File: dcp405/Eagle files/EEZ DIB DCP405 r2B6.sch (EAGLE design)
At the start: 316 parts, among them IC1 LTC3864EMSE#PBF, IC10 MC33272ADR2G, IC11 LTC2050HVCS8#PBF, IC12 74AUP1G74DC.125, IC13 MCP23S17-E/SS, IC14 TC77-5.0MCTTR, IC15 REF5025AIDR, IC16 DAC8552IDGKR, IC17 SN74LVC1G3157DCKR, IC18 ADS1120IPWR, IC19 LM339D, IC2 TPS54060DGQ, IC20 MAX9141ESA, IC3 SI8641BB-B-IS1, IC4 SN74LVC1G139DCUR, IC5 MC78L05, IC6 MC79L05, IC7 SI8641BB-B-IS1, IC8 M24C32-WMN6P, IC9 OPA2196ID, J1 4907, J2 FCR7350R, J3 FCR7350B, K1 G6K-2F-5DC, Q1 SUD19P06-60, Q10 BSS205NH6327XTSA1, Q11 PSMN0R9-25YLC, Q12 PSMN0R9-25YLC, Q13 BSS84P, Q14 BTA26-600, Q15 FMMT493TA, Q16 2N7002, Q17 2N7002, Q18 2N7002, Q19 MMBT5551, Q2 MMBT5401, Q20 MMBT5401, Q21 MMBT5551, Q22 MMBT5551, Q23 2N7002, Q3 D45H11, Q4 D45H11, Q5 BC856C, Q6 MMBT5401, Q7 STF10P6F6, Q8 BCP56-16.115, Q9 NZT605, Q9B BDX33C, X1 39-30-1020, X2 77317-104-28LF, X3 1844249, X4 DS1024-2*10R0

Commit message: DCP405 r2B6 (w/o BOM)
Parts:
- removed D20: SK10100D1-DIO, EEZ_Lib1:SCHOTTKY-DUAL_A_L
- removed D21: BAS316, EEZ_Lib1:DIODESOD323R
- removed JP2: JP3-CUT-ROTATED, EEZ_Lib1:JP3-CUT-ROTATED
- removed JP3: JP3-CUT, EEZ_Lib1:JP3-CUT
- removed Q23: 2N7002, EEZ_Lib1:2N7002
- removed Q9B: BDX33C, EEZ_Lib1:BDX33C
- removed R111: 750R, rcl:R-EU_R0805
- removed R112: 47K, rcl:R-EU_R0805
- removed R113: 330R, rcl:R-EU_R0805
- removed R114: 470R, rcl:R-EU_R0805
- removed R115: 100K, rcl:R-EU_R0805
- added C96: 10n, rcl:C-EUC0805
- added ZD3: SLVU2.8-TP, EEZ_Lib1:SLVU2.8
- C29: value 100n -> 10n; device rcl:C-EUC0603 -> rcl:C-EUC0805
- C41: value 47p -> 470p
- C43: value 470p -> 33p
- C44: value 2n2 -> 330p
- C45: value 220p -> 2n2
- C46: value 47p -> 33p
- C47: value 470p -> 10n
- C48, C70, C86: value 10n -> 100n; device rcl:C-EUC0805 -> rcl:C-EUC0603
- C51, C67, C77, C79: value 100n -> 1u; device rcl:C-EUC0603 -> rcl:C-EUC0805
- C52: value 1u -> 10n
- C53: value 10n -> 1n
- C54: value 1n -> 1u
- C55, C76, C78: value 1u -> 100n; device rcl:C-EUC0805 -> rcl:C-EUC0603
- C58: value 100n -> 33p; device rcl:C-EUC0603 -> rcl:C-EUC0805
- C60: value 100n -> 100p; device rcl:C-EUC0603 -> rcl:C-EUC0805
- C62: value 4u7 -> 100n; device rcl:C-EUC1206 -> rcl:C-EUC0603
- C63: value 100n -> 4u7; device rcl:C-EUC0603 -> rcl:C-EUC1206
- C64: value 4u7 tant. -> 100n; device EEZ_Lib1:ECAP1206 -> rcl:C-EUC0603
- C65: value 1u -> 4u7 tant.; device rcl:C-EUC0805 -> EEZ_Lib1:ECAP1206
- C71: value 4n7 -> 10n
- C75: value 100n -> 4n7; device rcl:C-EUC0603 -> rcl:C-EUC0805
- C84: value 100n -> 1n; device rcl:C-EUC0603 -> rcl:C-EUC0805
- C85: value 1n -> 100n; device rcl:C-EUC0805 -> rcl:C-EUC0603
- C87: value 2n2 -> 10n
- C88: value 470n -> 2n2; device rcl:C-EUC1206 -> rcl:C-EUC0805
- C89: value HHXC630ARA220MHA0G -> 470n; device EEZ_Lib1:ECAPSMD8.3MM/HA0 -> rcl:C-EUC1206
- C90: value 10n/200V -> HHXC630ARA220MHA0G; device rcl:C-EUC1206 -> EEZ_Lib1:ECAPSMD8.3MM/HA0
- C91: value N.C. -> 10n/200V; device EEZ_Lib1:ECAP2G/5 -> rcl:C-EUC1206
- C92: device rcl:C-EUC0805 -> EEZ_Lib1:ECAP2G/5
- C94: value 10n/200V -> N.C.; device rcl:C-EUC1206 -> rcl:C-EUC0805
- C95: value 10n -> 10n/200V; device rcl:C-EUC0805 -> rcl:C-EUC1206
- D10: value SKL14 -> BAS316; device EEZ_Lib1:SCHOTTKYSOD123 -> EEZ_Lib1:DIODESOD323R
- D12: value BAS316 -> SK55; device EEZ_Lib1:DIODESOD323R -> EEZ_Lib1:SCHOTTKYSMB
- D14: value SK55 -> BAS316; device EEZ_Lib1:SCHOTTKYSMB -> EEZ_Lib1:DIODESOD323R
- D18: value BAS316 -> SK10100D1-DIO; device EEZ_Lib1:DIODESOD323R -> EEZ_Lib1:SCHOTTKY-DUAL_A_L
- D8: value BAS316 -> SKL14; device EEZ_Lib1:DIODESOD323R -> EEZ_Lib1:SCHOTTKYSOD123
- IC14: value TC77-5.0MCTTR -> REF5025AIDR; device EEZ_Lib1:TC77 -> EEZ_Lib1:REF50XX
- IC15: value REF5025AIDR -> TC77-5.0MCTTR; device EEZ_Lib1:REF50XX -> EEZ_Lib1:TC77
- IC19: value LM339D -> LM293D; device EEZ_Lib1:LM339SO14 -> EEZ_Lib1:LM293D
- IC9: value OPA2196ID -> MC33272ADR2G
- Q10: value BSS205NH6327XTSA1 -> PSMN0R9-25YLC; device EEZ_Lib1:2N7002 -> EEZ_Lib1:N-MOSFETLFPAK; MPN 2N7002-7-F -> (none); OC_FARNELL 1713823 -> (none); OC_NEWARK 25R5679 -> (none); PACKAGE SOT-23-3 -> (none); SUPPLIER DIODES INC. -> (none)
- Q12: value PSMN0R9-25YLC -> BSS84P; device EEZ_Lib1:N-MOSFETLFPAK -> EEZ_Lib1:IRLML2246TRPBF
- Q13: value BSS84P -> BTA26-600; device EEZ_Lib1:IRLML2246TRPBF -> EEZ_Lib1:BTA41-2
- Q14: value BTA26-600 -> FMMT493TA; device EEZ_Lib1:BTA41-2 -> transistor:MMBT5551LT1-NPN-SOT23-BEC
- Q15: value FMMT493TA -> 2N7002; device transistor:MMBT5551LT1-NPN-SOT23-BEC -> EEZ_Lib1:2N7002
- Q17: MPN (none) -> 2N7002-7-F; OC_FARNELL (none) -> 1713823; OC_NEWARK (none) -> 25R5679; PACKAGE (none) -> SOT-23-3; SUPPLIER (none) -> DIODES INC.
- Q18: value 2N7002 -> MMBT5551; device EEZ_Lib1:2N7002 -> transistor:MMBT5551LT1-NPN-SOT23-BEC; MPN 2N7002-7-F -> (none); OC_FARNELL 1713823 -> (none); OC_NEWARK 25R5679 -> (none); PACKAGE SOT-23-3 -> (none); SUPPLIER DIODES INC. -> (none)
- Q19: value MMBT5551 -> MMBT5401; device transistor:MMBT5551LT1-NPN-SOT23-BEC -> transistor:BC857B-PNP-SOT23-BEC
- Q20: value MMBT5401 -> MMBT5551; device transistor:BC857B-PNP-SOT23-BEC -> transistor:MMBT5551LT1-NPN-SOT23-BEC
- Q22: value MMBT5551 -> 2N7002; device transistor:MMBT5551LT1-NPN-SOT23-BEC -> EEZ_Lib1:2N7002; MPN (none) -> 2N7002-7-F; OC_FARNELL (none) -> 1713823; OC_NEWARK (none) -> 25R5679; PACKAGE (none) -> SOT-23-3; SUPPLIER (none) -> DIODES INC.
- Q5: value BC856C -> STF10P6F6; device transistor:BC857C-PNP-SOT23-BEC -> EEZ_Lib1:P-MOSFET-VERT
- Q6: value MMBT5401 -> BCP56-16.115; device transistor:BC857B-PNP-SOT23-BEC -> EEZ_Lib1:BCP56
- Q7: value STF10P6F6 -> MMBT5401; device EEZ_Lib1:P-MOSFET-VERT -> transistor:BC857B-PNP-SOT23-BEC
- Q8: value BCP56-16.115 -> NZT605; device EEZ_Lib1:BCP56 -> EEZ_Lib1:NZT605
- Q9: value NZT605 -> BSS205NH6327XTSA1; device EEZ_Lib1:NZT605 -> EEZ_Lib1:2N7002; MPN (none) -> 2N7002-7-F; OC_FARNELL (none) -> 1713823; OC_NEWARK (none) -> 25R5679; PACKAGE (none) -> SOT-23-3; SUPPLIER (none) -> DIODES INC.
- R100: value 10K -> 750R
- R101: value N.C. -> 1K
- R102: value 330R -> 2K2
- R103, R104, R59: value 47K -> 10K
- R105: value 750R -> 1R
- R106: value 1K -> 750R
- R107: value 2K2 -> 47K
- R108: value 10K -> 330R
- R109, R69, R73: value 10K -> 470R
- R110: value 1R -> 100K
- R28: value 2R2/2W -> 0R1/2-3W
- R29: value 0R1/2-3W -> 2R2/2W
- R30: value 2K2 -> 4K7
- R31, R81, R93, R96: value 10K -> 4K7
- R32: value 10R -> 10K; device rcl:R-EU_R1206 -> rcl:R-EU_R0805
- R33: value 10R -> 2K2; device rcl:R-EU_R1206 -> rcl:R-EU_R0805
- R34, R78: value 2K2 -> 10R; device rcl:R-EU_R0805 -> rcl:R-EU_R1206
- R35: value 470R -> 10R; device rcl:R-EU_R0805 -> rcl:R-EU_R1206
- R36: value 220R -> 4K7
- R37: value 10R -> 5K6; device rcl:R-EU_R1206 -> rcl:R-EU_R0805
- R38: value 1R -> 220R
- R40: value 7K5 0.1% -> 220R
- R41: value 10K -> 7K5 0.1%
- R42: value 220R -> 22K
- R44: value 100K 0.1% -> 4K7
- R45: value 24K 0.1% -> 124K 0.1%
- R46: value 220R -> 124K 0.1%
- R49: value 7K5 0.1% -> 15R; device rcl:R-EU_R0805 -> rcl:R-EU_R1206
- R50: value 100K 0.1% -> 7K5 0.1%
- R51: value 24K 0.1% -> 36K
- R52: value 15R -> 4K7; device rcl:R-EU_R1206 -> rcl:R-EU_R0805
- R53: value 0R -> 100K
- R54: value 10K -> 39K 0.1%
- R55: value 220R -> 820R 0.1%
- R56: value 100K -> 47K
- R57: value 39K 0.1% -> 2K2
- R58: value 820R 0.1% -> 0R75; device rcl:R-EU_R0805 -> rcl:R-EU_R1206
- R60: value 2K2 -> 10K
- R61: value 0R75 -> 39K 0.1%; device rcl:R-EU_R1206 -> rcl:R-EU_R0805
- R62, R98: value 10K -> 47K
- R64: value 39K 0.1% -> 0R010 (low TCR); device rcl:R-EU_R0805 -> EEZ_Lib1:R-EU_4WIRE2512
- R65: value 47K -> 820R 0.1%
- R66: value 10K -> 1K
- R67: value 0R010 (low TCR) -> 10K; device EEZ_Lib1:R-EU_4WIRE2512 -> rcl:R-EU_R0805
- R68: value 820R 0.1% -> 100K
- R70: value 100K -> 270R
- R71, R74, R75: value 470R -> 2K2
- R72: value 270R -> 470R
- R79: value 2K2 -> 750R
- R80: value 10R -> 470R; device rcl:R-EU_R1206 -> rcl:R-EU_R0805
- R82: value 750R -> 10K
- R83: value 470R -> 4K7
- R84: value 5K1 -> 10K
- R85: value 47K -> 330R
- R86: value 5K6 -> 1K
- R87: value 10K -> AC01000001007JA100; device rcl:R-EU_R0805 -> rcl:R-EU_0411/15
- R89: value 1K -> 10K
- R90: value AC01000001007JA100 -> 100K; device rcl:R-EU_0411/15 -> rcl:R-EU_R0805
- R91: value 2K2 -> 6R2
- R92: value 330R -> 10K
- R94: value 100K -> 10K
- R95: value 6R2 -> 4K7
- R97: value 5K1 -> 330R
- R99: value 5K6 -> 47K
- ZD2: value SLVU2.8-TP -> 7V5; device EEZ_Lib1:SLVU2.8 -> EEZ_Lib1:ZENER-DIODESOD323
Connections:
- net N$55 renamed PASS_E1
- removed net !TEMP_CS: IC13.GPB5, IC14.!CS
- removed net +VAUX: X2-2.1
- removed net DIB_NFAULT: X2-3.1
- removed net DP_LED: Q13.D, R73.2
- removed net N$10: IC7.B4, RN2-4.1
- removed net N$117: C42.1, R44.2, R45.1
- removed net N$118: Q16.D, R88.2
- removed net N$147: D9.A, Q5.C, Q7.G, R34.2
- removed net N$177: IC19B.-IN, IC19D.-IN, R96.1, R98.2
- removed net N$44: D10.A, Q6.E, R32.1, R33.1
- removed net N$46: Q17.D, R92.1
- removed net N$53: JP2.NO, JP3.NO
- removed net N$54: IC20.!LE, JP3.COM
- removed net N$85: C44.1, R50.2, R51.1
- removed net N$86: C41.2, R41.1
- removed net N$87: C46.2, R54.1
- removed net N$99: Q5.B, R30.2
- removed net OVP_IO: IC13.GPA5, JP2.COM
- new net D_CC: Q16.D, R88.1
- new net D_CV: Q15.D, R85.2
- new net N$49: R30.1, R36.2
- new net N$55: C41.1, D9.A, Q7.B, R42.2
- new net PASS_E2: Q4.E, R28.2
- new net TEMP_CS: IC15.!CS, RN1-4.2
- net !DP_DRIVE: now also D8.A, Q7.E, R71.1; no longer Q8.B, R39.1, R73.1
- net !OVP_FAULT: now also D13.C, IC13.GPA5, Q17.D, R96.2; no longer D16.C, JP2.NC, Q18.D, R101.2
- net !RESET: now also C60.1, R66.2
- net !SET_DP: now also Q12.G, R68.2; no longer Q13.G, R70.2
- net +5V: now also C60.2, C62.1, C64.1, C77.2, D19.C, IC15.VDD, Q12.S, R103.2, R66.1, R67.1, R68.1, R81.2, R93.2; no longer C60.1, C63.1, C75.2, D21.C, IC14.VDD, Q13.S, R108.2, R69.1, R70.1, R84.2, R97.2
- net +VREF: now also C65.+, C69.2, C80.2, IC14.VOUT, R32.1; no longer C64.+, C68.2, C79.2, IC15.VOUT, R31.1
- net -12V: now also R40.2; no longer R42.2
- net 50MA_S: now also Q10.S, R55.1; no longer Q11.S, R61.1
- net 5A_S: now also Q11.S, R64.2; no longer Q12.S, R67.2
- net AUX_IN: now also C71.2, R72.1, ZD3.C; no longer C70.2, R74.1, ZD2.C
- net CC_ACTIVE: now also Q16.G, R93.1, R95.2; no longer Q17.G, R97.1, R99.2
- net CC_LED: now also R88.2; no longer R92.2
- net CURR_50MA: now also Q10.G, R56.2; no longer Q11.G, R59.2
- net CURR_5A: now also Q11.G, R62.2; no longer Q12.G, R65.2
- net CV_ACTIVE: now also Q15.G, R81.1, R83.2; no longer Q16.G, R84.1, R86.2
- net CV_LED: now also R85.1; no longer R88.1
- net DARL_C: now also Q8.C, R33.1, R34.1, R35.1; no longer Q9.C, Q9B.C, R37.1, R38.1
- net DP_S: now also Q5.S, R29.1; no longer Q7.S, R28.1, R30.1, R34.1
- net GCOM: now also R41.1, R54.1; no longer R40.1, R57.1
- net GND: now also C47.1, C48.2, C49.1, C54.1, C55.2, C56.1, C64.2, C65.-, C67.2, C69.1, C70.2, C73.1, C74.2, C86.1, D17.C, D8.C, D9.C, Q15.S, Q18.E, Q20.E, Q22.S, Q9.S, R107.1, R110.1, R38.2, R53.1, R62.1, R69.1, R70.2, R84.2, R90.1, R98.1, ZD3.A; no longer C48.1, C49.2, C53.1, C55.1, C56.2, C58.1, C60.2, C64.-, C65.2, C67.1, C69.2, C70.1, C73.2, C74.1, D19.C, Q10.S, Q18.S, Q19.E, Q21.E, Q23.S, R103.1, R112.1, R115.1, R36.2, R59.1, R65.1, R71.1, R72.2, R87.2, R94.1, R95.1, R96.2, ZD2.A
- net IRQ: now also IC7.B4; no longer RN2-4.2
- net ISENSE+: now also R54.2, R55.2; no longer R57.2, R58.2
- net ISENSE-: now also R61.1, R65.2; no longer R64.1, R68.2
- net I_MON: now also R59.1, R61.2, R77.1; no longer R62.1, R64.2, R79.1
- net I_SERVO: now also C53.2, C58.2, D11.C, R94.1; no longer C54.2, D13.C, D15.A, R100.1
- net I_SET: now also R57.1, R74.1; no longer R60.1, R76.1
- net LOOP_CTRL: now also D10.A, Q8.B, R92.2; no longer D13.A, Q9.B, Q9B.B
- net MISO: now also IC15.SI/O, RN2-2.2; no longer IC14.SI/O, RN2-1.2
- net MOSI: now also RN2-3.2; no longer RN2-2.2
- net N$102: now also R32.2, R38.1; no longer R31.2, R36.1
- net N$105: now also R83.1; no longer IC19B.OUT, R86.1
- net N$106: now also IC19B.OUT, R95.1; no longer IC19C.OUT, IC19D.OUT, R99.1
- net N$107: now also C87.2, Q19.B, R100.2, R102.2, R97.1; no longer C86.2, Q20.B, R102.1, R105.2, R107.2
- net N$108: now also C88.2, Q19.C, R104.2, R99.1; no longer C87.2, Q20.C, R104.1, R109.2
- net N$109: now also Q21.C, R101.1; no longer Q22.C, R106.1
- net N$11: now also R58.2, R64.2S; no longer R61.2, R67.2S
- net N$110: now also C96.1, Q21.B, R106.1, R108.2; no longer C95.1, Q22.B, R111.1, R113.2
- net N$111: now also C88.1, Q18.B, R98.2, R99.2; no longer C87.1, Q19.B, R103.2, R104.2
- net N$112: now also Q20.B, R104.1, R107.2; no longer Q21.B, R109.1, R112.2
- net N$113: now also C89.2, R105.2; no longer C88.2, R110.2
- net N$114: now also D19.A, Q22.D, R109.1; no longer D21.A, Q23.D, R114.1
- net N$12: now also R70.1; no longer R72.1
- net N$120: now also R109.2; no longer R114.2
- net N$121: now also R69.2; no longer R71.2
- net N$122: now also RN2-1.1; no longer RN1-4.1
- net N$13: now also Q17.G, R86.2; no longer Q18.G, R89.2
- net N$14: now also C44.1, R51.2; no longer C45.1, R53.2
- net N$15: now also Q13.A2, R87.2; no longer Q14.A2, R90.2
- net N$150: now also R45.1; no longer R40.2, R44.1
- net N$153: now also R82.2; no longer IC19B.+IN, R81.2
- net N$158: now also C43.1, R46.1, R50.2; no longer R49.2, R50.1, R54.2
- net N$161: now also IC19B.-IN, R94.2; no longer IC19C.-IN, IC19D.+IN, R100.2
- net N$17: now also R72.2, R73.1; no longer R74.2, R75.1
- net N$170: now also IC19B.+IN, R92.1; no longer IC19C.+IN, R85.1, R91.2
- net N$173: now also R101.2, R102.1; no longer R106.2, R107.1
- net N$18: now also Q13.G, Q14.C, R80.1; no longer Q14.G, Q15.C, R83.1
- net N$19: now also Q14.E, R91.2; no longer Q15.E, R95.2
- net N$20: now also D16.C, D17.A; no longer D18.C, D19.A
- net N$200: now also R64.1S, R65.1; no longer R67.1S, R68.1
- net N$21: now also D16.A, Q14.B, R86.1, R90.2; no longer D18.A, Q15.B, R89.1, R94.2
- net N$3: now also RN2-4.1; no longer RN2-3.1
- net N$31: now also C84.2, R89.2; no longer C85.2, R93.2
- net N$32: now also R73.2; no longer R75.2
- net N$33: now also R79.2, R84.1; no longer R82.2, R87.1
- net N$35: now also Q9.D, R49.1; no longer Q10.D, R52.1
- net N$37: now also C53.1, R60.1; no longer C54.1, R63.1
- net N$39: now also R37.1, R39.1; no longer R37.2
- net N$40: now also R35.2; no longer R33.2
- net N$42: now also Q12.D, R71.2; no longer Q4.E, R29.2
- net N$43: now also R34.2; no longer R32.2
- net N$45: now also C41.2, Q7.C, R37.2; no longer Q6.C, R35.2
- net N$47: now also Q8.E, R49.2; no longer Q9.E, Q9B.E, R52.2
- net N$52: now also IC4.Y3, RN1-4.1; no longer D10.C, R38.2
- net N$56: now also D13.A, D14.A, D15.A, R67.2; no longer D16.A, D17.A, R69.2
- net N$61: now also RN2-3.1; no longer RN2-2.1
- net N$70: now also C79.2, R78.2; no longer C77.2, R80.2
- net N$71: now also C67.1, IC14.TRIM/NR; no longer C66.1, IC15.TRIM/NR
- net N$72: now also C72.2, R74.2; no longer C71.2, R76.2
- net N$73: now also C75.2, R76.2; no longer C74.2, R78.2
- net N$80: now also C73.2, R75.2; no longer C72.2, R77.2
- net N$81: now also C74.1, R77.2; no longer C73.1, R79.2
- net N$82: now also R57.2; no longer R60.2
- net N$83: now also R44.2; no longer R46.2
- net N$84: now also C46.1, R51.1, R52.2; no longer D12.C, R53.1, R55.2
- net N$88: now also R63.1; no longer R66.1
- net N$89: now also C58.1, R59.2, R60.2; no longer D15.C, R62.2, R66.2
- net N$9: now also RN2-2.1; no longer RN2-1.1
- net N$90: now also C42.2, R44.1; no longer C43.2, R46.1
- net N$91: now also C45.2, R52.1; no longer C47.2, R55.1
- net N$98: now also Q6.E, R40.1; no longer Q8.E, R42.1
- net OE_TRIG: now also RN2-4.2; no longer RN2-3.2
- net OUTC+: now also C91.1, C92.+, C94.1; no longer C90.1, C91.+, C92.1
- net OUTC-: now also C92.-, C95.2; no longer C91.-, C92.2
- net OUTF+: now also Q13.A1, R80.2; no longer Q14.A1, R83.2
- net PE: now also C91.2, C95.1; no longer C90.2, C94.1
- net POST_OE: now also Q9.G, R53.2; no longer Q10.G, R56.2
- net POST_OUT+: now also C45.1, R29.2, R30.2, R31.1, ZD2.C; no longer C42.2, C47.1, D8.A, Q5.E, R28.2
- net POST_OUT-: now also C42.1, C90.-, C96.2, D12.A, D18.A, Q10.D, Q21.E, R105.1, R108.1; no longer C43.1, C44.2, C89.-, C95.2, D14.A, D20.A, Q12.D, Q22.E, R110.1, R113.1
- net POST_OUTF+: now also C87.1, C89.1, C90.+, D18.C, Q19.E, R97.2; no longer C86.1, C88.1, C89.+, D20.C, Q20.E, R102.2
- net PREG_OUT+: now also R28.1, R33.2; no longer R29.1
- net PREG_OUT-: now also D12.C, Q5.D, R36.1, R64.1, R87.1; no longer D14.C, Q7.D, R67.1, R90.1
- net PWRGOOD: now also D15.C
- net Q6C: now also Q5.G, Q6.C, R31.2, ZD2.A; no longer D8.C, D9.C, Q8.C, R35.1
- net RSENSE: now also Q22.G, R110.2; no longer Q23.G, R115.2
- net SCLK: now also IC15.SCLK, RN2-1.2; no longer IC14.SCLK, RN1-4.2
- net SENSE+: now also R100.1; no longer C41.1, R105.1
- net SENSE-: now also R106.2, R46.2; no longer C46.1, R111.2, R51.2
- net SENSE_ERR: now also Q20.C, R103.1; no longer Q21.C, R108.1
- net SENSE_PROT: now also D14.C, Q18.C; no longer D17.C, Q19.C
- net U_MON: now also C43.2, R50.1, R76.1, R79.1; no longer R49.1, R78.1, R82.1
- net U_SERVO: now also C44.2, C46.2, D10.C, R42.1, R82.1; no longer C45.2, D11.C, D12.A, R81.1
- net U_SET: now also R75.1, R89.1; no longer R77.1, R93.1
- net V+: now also C47.2, C48.1, C49.2, C63.1, C66.1, C68.2, C70.1, C85.2, IC14.VIN, IC20.!LE, R78.1, R96.1; no longer C48.2, C49.1, C52.2, C62.1, C65.1, C67.2, C69.1, C80.2, IC15.VIN, JP3.NC, R101.1, R80.1, R85.2
- net V-: now also C52.2, C54.2, C55.1, C56.2, C86.2, IC19P.V-; no longer C53.2, C55.2, C56.1, C58.2, C84.2, IC19P.GND, R98.1
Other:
- note added: "-"
- note added: "Note 3.1: Q3, Q4 and Q5 mounted on heatsink"
- note added: "OVP Fault"
- note removed: "+0.275 V"
- note removed: "-2.32 V"
- note removed: "Note 3.1: Q3, Q4 and Q6 mounted on heatsink"
- note removed: "OVP Ctrl"
- note removed: "Temp sensor CS"
- moved on the sheet: C41, C42, C43, C44, C45, C46, C47, C48, C49, C50, C51, C52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

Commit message: DCP405 r2B6 BOM
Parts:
- C53: value 1n -> 6n8
- C59: value 470p -> 1n
- C60: value 100p -> 120p
- R58: value 0R75 -> 1R
- R60: value 10K -> 330K
- ZD2: value 7V5 -> MM3Z9V1T1G
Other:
- note added: "Current control loop"
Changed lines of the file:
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@@
 <setting verticaltext="up"/>
 </settings>
-<grid distance="0.025" unitdist="inch" unit="inch" style="lines" multiple="4" display="no" altdistance="0.01" altunitdist="inch" altunit="inch"/>
+<grid distance="0.1" unitdist="inch" unit="inch" style="lines" multiple="1" display="no" altdistance="0.01" altunitdist="inch" altunit="inch"/>
 <layers>
 <layer number="1" name="Top" color="4" fill="1" visible="no" active="no"/>
@@
 <part name="P+5" library="supply2" deviceset="V+" device=""/>
 <part name="C49" library="rcl" deviceset="C-EU" device="C0603" value="100n"/>
-<part name="C53" library="rcl" deviceset="C-EU" device="C0805" value="1n"/>
+<part name="C53" library="rcl" deviceset="C-EU" device="C0805" value="6n8"/>
 <part name="R59" library="rcl" deviceset="R-EU_" device="R0805" value="10K"/>
 <part name="R57" library="rcl" deviceset="R-EU_" device="R0805" value="2K2"/>
@@
 <part name="R48" library="rcl" deviceset="R-EU_" device="R0805" value="10K"/>
 <part name="FRAME1" library="frames" deviceset="DINA4_L" device=""/>
-<part name="R60" library="rcl" deviceset="R-EU_" device="R0805" value="10K"/>
+<part name="R60" library="rcl" deviceset="R-EU_" device="R0805" value="330K"/>
 <part name="R63" library="rcl" deviceset="R-EU_" device="R0805" value="10K"/>
-<part name="C59" library="rcl" deviceset="C-EU" device="C0805" value="470p"/>
+<part name="C59" library="rcl" deviceset="C-EU" device="C0805" value="1n"/>
 <part name="C42" library="rcl" deviceset="C-EU" device="C0805" value="2n2"/>
 <part name="R44" library="rcl" deviceset="R-EU_" device="R0805" value="4K7"/>
@@
 <part name="SUPPLY102" library="supply2" deviceset="GND" device="" value="GND"/>
 <part name="Q10" library="EEZ_Lib1" deviceset="N-MOSFET" device="LFPAK" value="PSMN0R9-25YLC"/>
-<part name="R58" library="rcl" deviceset="R-EU_" device="R1206" value="0R75"/>
+<part name="R58" library="rcl" deviceset="R-EU_" device="R1206" value="1R"/>
 <part name="R56" library="rcl" deviceset="R-EU_" device="R0805" value="47K"/>
 <part name="SUPPLY128" library="supply2" deviceset="GND" device="" value="GND"/>
@@
 <part name="IC19" library="EEZ_Lib1" deviceset="LM293" device="D"/>
 <part name="R33" library="rcl" deviceset="R-EU_" device="R0805" value="2K2"/>
-<part name="ZD2" library="EEZ_Lib1" deviceset="ZENER-DIODE" device="SOD323" value="7V5"/>
+<part name="ZD2" library="EEZ_Lib1" deviceset="ZENER-DIODE" device="SOD323" value="MM3Z9V1T1G"/>
 <part name="P+6" library="supply1" deviceset="+5V" device=""/>
 <part name="R66" library="rcl" deviceset="R-EU_" device="R0805" value="1K"/>
-<part name="C60" library="rcl" deviceset="C-EU" device="C0805" value="100p"/>
+<part name="C60" library="rcl" deviceset="C-EU" device="C0805" value="120p"/>
 <part name="R71" library="rcl" deviceset="R-EU_" device="R0805" value="2K2"/>
 <part name="D15" library="EEZ_Lib1" deviceset="DIODE" device="SOD323R" value="BAS316"/>
@@
 <description>Post-regulator</description>
 <plain>
-<text x="115.57" y="106.045" size="1.778" layer="97">Voltage control loop</text>
+<text x="107.95" y="106.045" size="1.778" layer="97">Voltage control loop</text>
 <text x="165.1" y="98.425" size="1.27" layer="103">U_SET (+2.5V for full range)</text>
 <wire x1="185.42" y1="109.22" x2="106.68" y2="109.22" width="0.1524" layer="97" style="shortdash"/>
-<wire x1="106.68" y1="109.22" x2="106.68" y2="58.42" width="0.1524" layer="97" style="shortdash"/>
+<wire x1="106.68" y1="109.22" x2="106.68" y2="73.66" width="0.1524" layer="97" style="shortdash"/>
+<wire x1="106.68" y1="73.66" x2="106.68" y2="58.42" width="0.1524" layer="97" style="shortdash"/>
 <wire x1="238.76" y1="127" x2="238.76" y2="166.37" width="0.1524" layer="97" style="shortdash"/>
 <text x="5.08" y="15.24" size="1.4224" layer="103">Note 3.1: Q3, Q4 and Q5 mounted on heatsink</text>
@@
 <wire x1="185.42" y1="166.37" x2="185.42" y2="127" width="0.1524" layer="97" style="shortdash"/>
 <wire x1="185.42" y1="127" x2="185.42" y2="109.22" width="0.1524" layer="97" style="shortdash"/>
-<text x="113.03" y="163.195" size="1.778" layer="97">Down-programmer</text>
+<text x="107.95" y="163.195" size="1.778" layer="97">Down-programmer</text>
 <wire x1="106.68" y1="166.37" x2="185.42" y2="166.37" width="0.1524" layer="97" style="shortdash"/>
 <wire x1="83.82" y1="58.42" x2="83.82" y2="5.08" width="0.1524" layer="97" style="shortdash"/>
@@
 <text x="200.66" y="1.905" size="2.54" layer="94" font="vector" rot="MR0">- Date:</text>
 <text x="76.835" y="171.45" size="1.27" layer="103">See Note 3.1</text>
-<rectangle x1="115.57" y1="21.59" x2="127.635" y2="29.21" layer="97"/>
+<text x="107.95" y="70.485" size="1.778" layer="97">Current control loop</text>
+<wire x1="106.68" y1="73.66" x2="238.76" y2="73.66" width="0.1524" layer="97" style="shortdash"/>
 </plain>
 <instances>
@@
 <instance part="ZD2" gate="G$1" x="160.02" y="152.4" smashed="yes" rot="R90">
 <attribute name="NAME" x="162.052" y="153.035" size="1.778" layer="95"/>
-<attribute name="VALUE" x="162.052" y="150.876" size="1.778" layer="96"/>
+<attribute name="VALUE" x="162.052" y="150.876" size="1.27" layer="96"/>
 </instance>
 <instance part="Q7" gate="G$1" x="119.38" y="137.16" smashed="yes" rot="R90">
@@
 </instance>
 <instance part="D8" gate="G$1" x="111.76" y="134.62" smashed="yes" rot="R270">
-<attribute name="NAME" x="110.236" y="133.985" size="1.778" layer="95" rot="R180"/>
-<attribute name="VALUE" x="110.236" y="136.144" size="1.778" layer="96" rot="R180"/>
+<attribute name="NAME" x="110.236" y="136.525" size="1.778" layer="95" rot="R180"/>
+<attribute name="VALUE" x="110.236" y="134.239" size="1.778" layer="96" rot="R180"/>
 </instance>
 <instance part="D9" gate="G$1" x="127" y="127" smashed="yes" rot="R270">
@@
 </segment>
 <segment>
-<wire x1="223.52" y1="76.2" x2="241.3" y2="76.2" width="0.4064" layer="91"/>
+<wire x1="223.52" y1="71.12" x2="241.3" y2="71.12" width="0.4064" layer="91"/>
 <wire x1="223.52" y1="43.18" x2="223.52" y2="48.26" width="0.4064" layer="91"/>
 <pinref part="Q11" gate="G$1" pin="D"/>
-<wire x1="223.52" y1="48.26" x2="223.52" y2="76.2" width="0.4064" layer="91"/>
+<wire x1="223.52" y1="48.26" x2="223.52" y2="71.12" width="0.4064" layer="91"/>
 <pinref part="Q10" gate="G$1" pin="D"/>
-<wire x1="223.52" y1="76.2" x2="210.82" y2="76.2" width="0.4064" layer="91"/>
-<wire x1="210.82" y1="76.2" x2="210.82" y2="68.58" width="0.4064" layer="91"/>
+<wire x1="223.52" y1="71.12" x2="210.82" y2="71.12" width="0.4064" layer="91"/>
+<wire x1="210.82" y1="71.12" x2="210.82" y2="68.58" width="0.4064" layer="91"/>
 <pinref part="D12" gate="G$1" pin="A"/>
 <wire x1="223.52" y1="48.26" x2="231.14" y2="48.26" width="0.4064" layer="91"/>
 <wire x1="231.14" y1="48.26" x2="231.14" y2="33.02" width="0.4064" layer="91"/>
 <junction x="223.52" y="48.26"/>
-<junction x="223.52" y="76.2"/>
-<label x="257.81" y="76.2" size="1.27" layer="102" rot="R180" xref="yes"/>
+<junction x="223.52" y="71.12"/>
+<label x="257.81" y="71.12" size="1.27" layer="102" rot="R180" xref="yes"/>
 </segment>
 </net>

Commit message: DCP405 BOM update
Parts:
- removed C27: 22u, rcl:C-EUC1206
- removed JP5: JP2-CUT, EEZ_Lib1:JP2-CUT
- added JP2, JP3: JP2-CUT, EEZ_Lib1:JP2-CUT
- C2, C90: value HHXC630ARA220MHA0G -> HHXC630A330MHA0G
- C26: device rcl:C-EUC1206 -> rcl:C-EUC1210
- Q3, Q4: value D45H11 -> D45H11FP
- Q5: value STF10P6F6 -> FQPF11P06 or FQPF27P06
- R29: value 2R2/2W -> 4K7; device rcl:R-EU_R2512 -> rcl:R-EU_R0805
- R30: value 4K7 -> 2R2/2W; device rcl:R-EU_R0805 -> rcl:R-EU_R2512
- R33: value 2K2 -> 4K7
- R34: value 10R -> 2K2; device rcl:R-EU_R1206 -> rcl:R-EU_R0805
- R36: value 4K7 -> 10R; device rcl:R-EU_R0805 -> rcl:R-EU_R1206
- ZD2: device EEZ_Lib1:ZENER-DIODESOD323 -> EEZ_Lib1:ZENER-DIODESOD323R
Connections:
- new net !IOEXP_RST: C60.1, IC13.!RESET, JP1.2, R66.2
- net !RESET: now also JP1.1; no longer C60.1, IC13.!RESET, R66.2
- net DARL_C: now also R36.1; no longer R33.1
- net DP_S: now also R30.1; no longer R29.1
- net GND: no longer C27.2
- net N$40: now also R36.2; no longer R35.2
- net N$43: now also R35.2; no longer R34.2
- net N$49: now also R29.1, R33.2; no longer R30.1, R36.2
- net POST_OUT-: now also JP4.1; no longer JP5.1
- net POST_OUTF+: now also JP3.2; no longer JP4.2
- net PREG_OUT+: now also R34.2; no longer R33.2
- net PREG_OUT-: now also R33.1; no longer R36.1
- net SENSE+: now also JP3.1; no longer JP4.1
- net SENSE-: now also JP4.2; no longer JP5.2
- net U_SET: now also JP2.1; no longer JP1.1
- net U_SET_OUT: now also JP2.2; no longer JP1.2
- net VOUT+: no longer C27.1
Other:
- moved on the sheet: JP1, JP4, R29, R30, R33, R34, R35, R36

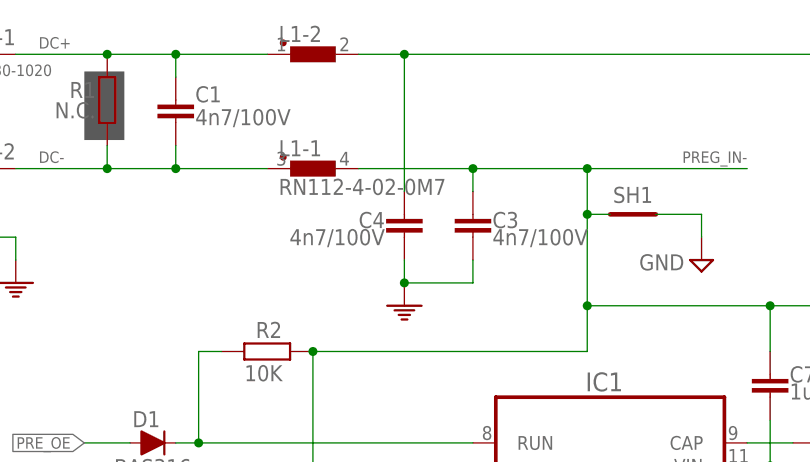
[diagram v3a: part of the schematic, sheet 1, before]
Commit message: DCP405 CC comp correction
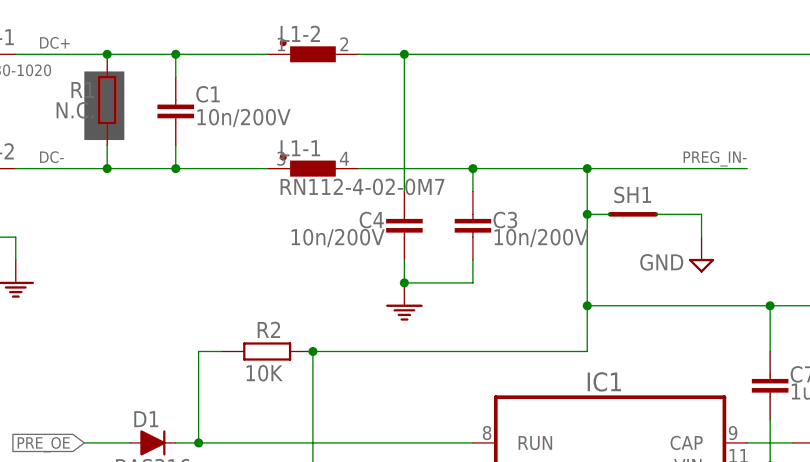
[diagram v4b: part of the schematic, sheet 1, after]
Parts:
- C1, C3, C4: value 4n7/100V -> 10n/200V
- R60: value 330K -> 1K
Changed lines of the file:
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@@
 <part name="R48" library="rcl" deviceset="R-EU_" device="R0805" value="10K"/>
 <part name="FRAME1" library="frames" deviceset="DINA4_L" device=""/>
-<part name="R60" library="rcl" deviceset="R-EU_" device="R0805" value="330K"/>
+<part name="R60" library="rcl" deviceset="R-EU_" device="R0805" value="1K"/>
 <part name="R63" library="rcl" deviceset="R-EU_" device="R0805" value="10K"/>
 <part name="C59" library="rcl" deviceset="C-EU" device="C0805" value="1n"/>
@@
 <part name="C19" library="rcl" deviceset="C-EU" device="C0805" value="470p"/>
 <part name="FB2" library="EEZ_Lib1" deviceset="FERRITE_BEAD" device="0603" value="60R@100MHz"/>
-<part name="C4" library="rcl" deviceset="C-EU" device="C1206" value="4n7/100V"/>
-<part name="C3" library="rcl" deviceset="C-EU" device="C1206" value="4n7/100V"/>
-<part name="C1" library="rcl" deviceset="C-EU" device="C1206" value="4n7/100V"/>
+<part name="C4" library="rcl" deviceset="C-EU" device="C1206" value="10n/200V"/>
+<part name="C3" library="rcl" deviceset="C-EU" device="C1206" value="10n/200V"/>
+<part name="C1" library="rcl" deviceset="C-EU" device="C1206" value="10n/200V"/>
 <part name="L2" library="EEZ_inductors_and_transformers" deviceset="125CDMCC/DS" device="" value="125CDMCCDS-330MC"/>
 <part name="C11" library="EEZ_Lib1" deviceset="ECAP" device="10X10" value="EEEFK1J101P"/>
